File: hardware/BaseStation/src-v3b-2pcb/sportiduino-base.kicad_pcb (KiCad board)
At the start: 2 copper layers, 73 x 45 mm, 46 parts, among them SW1 SW_Reed, X1 Battery, X2 Prog, X3 RC522, X4 MINI RC522, X5 Charge

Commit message: Files for JLCPCB assemble
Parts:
- added  : hole, Sportiduino:hole, F.Cu at (196.0, 107.4)
- added  : hole, Sportiduino:hole, F.Cu at (190.0, 103.4)
- added  : hole, Sportiduino:hole, F.Cu at (191.5, 103.4)
- added  : hole, Sportiduino:hole, F.Cu at (193.0, 103.4)
- added  : hole, Sportiduino:hole, F.Cu at (194.5, 103.4)
- added  : hole, Sportiduino:hole, F.Cu at (196.0, 103.4)
- added  : hole, Sportiduino:hole, F.Cu at (172.0, 107.4)
- added  : hole, Sportiduino:hole, F.Cu at (170.5, 107.4)
- added  : hole, Sportiduino:hole, F.Cu at (169.0, 107.4)
- added  : hole, Sportiduino:hole, F.Cu at (167.5, 107.4)
- added  : hole, Sportiduino:hole, F.Cu at (166.0, 107.4)
- added  : hole, Sportiduino:hole, F.Cu at (194.5, 107.4)
- added  : hole, Sportiduino:hole, F.Cu at (164.5, 107.4)
- added  : hole, Sportiduino:hole, F.Cu at (163.0, 107.4)
- added  : hole, Sportiduino:hole, F.Cu at (163.0, 103.4)
- added  : hole, Sportiduino:hole, F.Cu at (164.5, 103.4)
- added  : hole, Sportiduino:hole, F.Cu at (166.0, 103.4)
- added  : hole, Sportiduino:hole, F.Cu at (167.5, 103.4)
- added  : hole, Sportiduino:hole, F.Cu at (169.0, 103.4)
- added  : hole, Sportiduino:hole, F.Cu at (170.5, 103.4)
- added  : hole, Sportiduino:hole, F.Cu at (172.0, 103.4)
- added  : hole, Sportiduino:hole, F.Cu at (193.0, 107.4)
- added  : hole, Sportiduino:hole, F.Cu at (191.5, 107.4)
- added  : hole, Sportiduino:hole, F.Cu at (190.0, 107.4)
- added  : hole, Sportiduino:hole, F.Cu at (188.5, 107.4)
- added  : hole, Sportiduino:hole, F.Cu at (187.0, 107.4)
- added  : hole, Sportiduino:hole, F.Cu at (187.0, 103.4)
- added  : hole, Sportiduino:hole, F.Cu at (188.5, 103.4)
- added BZ1: TR1205Y, Buzzer_Beeper:MagneticBuzzer_ProSignal_ABT-410-RC, F.Cu at (200.0, 122.4)
- added C1: 100 nF, Capacitor_SMD:C_0805_2012Metric_Pad1.15x1.40mm_HandSolder, F.Cu at (160.5, 113.5)
- added C10: 100 nF, Capacitor_SMD:C_0805_2012Metric_Pad1.15x1.40mm_HandSolder, F.Cu at (164.0, 146.7)
- added C11: 10 uF, Capacitor_SMD:C_0805_2012Metric_Pad1.18x1.45mm_HandSolder, F.Cu at (197.3, 146.2)
- added C12: 10 uF, Capacitor_SMD:C_0805_2012Metric_Pad1.18x1.45mm_HandSolder, F.Cu at (186.0, 146.0)
- added C2: 4.7 uF, Capacitor_SMD:C_0805_2012Metric_Pad1.15x1.40mm_HandSolder, F.Cu at (181.0, 146.0)
- added C3: 4.7 uF, Capacitor_SMD:C_0805_2012Metric_Pad1.15x1.40mm_HandSolder, F.Cu at (175.0, 146.0)
- added C4: 100 nF, Capacitor_SMD:C_0805_2012Metric_Pad1.15x1.40mm_HandSolder, F.Cu at (161.8, 122.7)
- added C5: 100 nF, Capacitor_SMD:C_0805_2012Metric_Pad1.15x1.40mm_HandSolder, F.Cu at (148.8, 130.9)
- added C6: 100 nF, Capacitor_SMD:C_0805_2012Metric_Pad1.15x1.40mm_HandSolder, F.Cu at (148.8, 133.2)
- added C7: 100 nF, Capacitor_SMD:C_0805_2012Metric_Pad1.15x1.40mm_HandSolder, F.Cu at (153.8, 135.7)
- added C9: 100 nF, Capacitor_SMD:C_0805_2012Metric_Pad1.15x1.40mm_HandSolder, F.Cu at (161.5, 145.4)
- added D1: MCP1700-3302E, Package_TO_SOT_SMD:SOT-23_Handsoldering, F.Cu at (178.0, 145.7)
- added D2: ATmega328P-AU, Package_QFP:TQFP-32_7x7mm_P0.8mm, F.Cu at (156.0, 127.4)
- added D3: DS3231SN, Sportiduino:SOIC-16W_7.5x10.3mm_P1.27mm, F.Cu at (154.0, 145.5)
- added D4: 24LC256T-I/SN, Package_SO:SOIC-8_3.9x4.9mm_P1.27mm, F.Cu at (169.3, 146.2)
- added D5: TP4056, Sportiduino:TP4056_SOP-8-PP, F.Cu at (192.0, 146.7)
- added G***: LOGO, Sportiduino:logo, F.Cu at (175.8, 126.4)
- added R1: 10K, Resistor_SMD:R_0805_2012Metric_Pad1.15x1.40mm_HandSolder, F.Cu at (166.8, 140.0)
- added R10: 68K, Resistor_SMD:R_0805_2012Metric_Pad1.15x1.40mm_HandSolder, F.Cu at (145.0, 147.8)
- added R11: 3K3, Resistor_SMD:R_0805_2012Metric_Pad1.15x1.40mm_HandSolder, F.Cu at (145.5, 143.4)
- added R12: 1K, Resistor_SMD:R_0805_2012Metric_Pad1.20x1.40mm_HandSolder, B.Cu at (140.3, 135.9)
- added R13: 1K, Resistor_SMD:R_0805_2012Metric_Pad1.20x1.40mm_HandSolder, B.Cu at (140.3, 138.2)
- added R14: 3K3, Resistor_SMD:R_0805_2012Metric_Pad1.20x1.40mm_HandSolder, F.Cu at (197.3, 150.2)
- added R2: 100, Resistor_SMD:R_0805_2012Metric_Pad1.15x1.40mm_HandSolder, F.Cu at (141.8, 140.9)
- added R3: 10K, Resistor_SMD:R_0805_2012Metric_Pad1.15x1.40mm_HandSolder, F.Cu at (166.8, 142.1)
- added R4: 3K3, Resistor_SMD:R_0805_2012Metric_Pad1.15x1.40mm_HandSolder, F.Cu at (189.0, 110.5)
- added R5: 33K, Resistor_SMD:R_0805_2012Metric_Pad1.15x1.40mm_HandSolder, F.Cu at (191.4, 110.5)
- added R6: 33K, Resistor_SMD:R_0805_2012Metric_Pad1.15x1.40mm_HandSolder, F.Cu at (163.5, 119.2)
- added R8: 3K3, Resistor_SMD:R_0805_2012Metric_Pad1.15x1.40mm_HandSolder, F.Cu at (145.5, 141.4)
- added R9: 270K, Resistor_SMD:R_0805_2012Metric_Pad1.15x1.40mm_HandSolder, F.Cu at (145.0, 149.9)
- added REF**: hole, hole, F.Cu at (0.00, 0.00)
- added SW1: SW_Reed, Button_Switch_THT:SW_reed, B.Cu at (170.0, 109.5)
- added TP1: , TestPoint:TestPoint_THTPad_D1.5mm_Drill0.7mm, F.Cu at (147.5, 135.7)
- added TP2: , TestPoint:TestPoint_THTPad_D1.5mm_Drill0.7mm, F.Cu at (147.5, 138.7)
- added TP4: , TestPoint:TestPoint_THTPad_D1.5mm_Drill0.7mm, F.Cu at (160.3, 119.9)
- added TP5: , TestPoint:TestPoint_THTPad_D1.5mm_Drill0.7mm, F.Cu at (157.8, 119.9)
- added VD1: 3mm, LED_THT:LED_D3.0mm, B.Cu at (138.0, 143.3)
- added VD2: , LED_SMD:LED_0805_2012Metric_Pad1.15x1.40mm_HandSolder, B.Cu at (136.0, 135.9)
- added VD3: , LED_SMD:LED_0805_2012Metric_Pad1.15x1.40mm_HandSolder, B.Cu at (136.0, 138.2)
- added VT1: BSS138, Package_TO_SOT_SMD:SOT-23_Handsoldering, F.Cu at (195.9, 110.5)
- added X1: Battery, Connector_JST:JST_XH_B2B-XH-A_1x02_P2.50mm_Vertical, F.Cu at (203.5, 140.4)
- added X2: Prog, Connector_IDC:IDC-Header_2x05_P2.54mm_Vertical, F.Cu at (139.6, 131.9)
- added X3: RC522, Connector_PinHeader_2.54mm:PinHeader_1x08_P2.54mm_Vertical, B.Cu at (144.8, 138.9)
- added X4: MINI RC522, Connector_PinHeader_2.54mm:PinHeader_1x08_P2.54mm_Vertical, B.Cu at (167.0, 137.4)
- added X5: Charge, Connector_JST:JST_XH_B2B-XH-A_1x02_P2.50mm_Vertical, F.Cu at (203.5, 129.9)
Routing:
- net (no net): track 0.00 -> 1303.1 mm, vias 0 -> 76
- added copper zone on B.Cu, net (none)
- added copper zone on F.Cu, net (none)
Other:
- board size 73 x 45 mm -> 73 x 94 mm

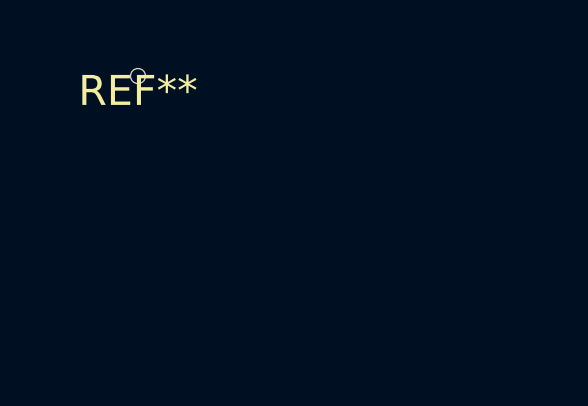
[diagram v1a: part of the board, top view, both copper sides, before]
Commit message: Updated BOM and pos files for BS PCB assembly
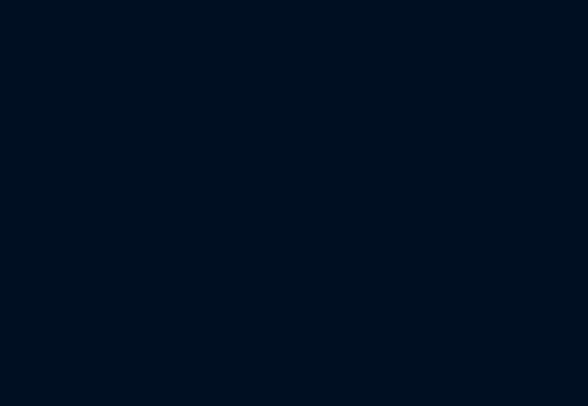
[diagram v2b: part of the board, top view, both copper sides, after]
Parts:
- removed REF**: hole, hole
- BZ1 (x2): value TR1205Y -> Passive Buzzer 12085 (12x8.5mm) 16 Ohm
- R14 (x2): value 3K3 -> 3K
- SW1 (x2): value SW_Reed -> Reed Switch Normally Open 2x14mm
- TP1 (x2), TP2 (x2), TP4 (x2), TP5 (x2): value (none) -> TestPoint (empty)
- VD1: value 3mm -> 1210 3528 BLUE 3.5x2.8x1.9mm
- VD1: value 3mm -> 1210 3528 BLUE 3.5*2.8*1.9mm
- VD2 (x2): value (none) -> 0805 GREEN
- VD3 (x2): value (none) -> 0805 RED
- X3 (x2): value RC522 -> Empty (RC522)
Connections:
- BZ1 pad 1: (no net) -> +BATT
- BZ1 pad 2: (no net) -> Net-(BZ1-Pad2)
- C1 pad 1: (no net) -> RST
- C1 pad 2: (no net) -> Net-(C1-Pad2)
- C10 pad 1: (no net) -> PD6
- C10 pad 2: (no net) -> GNDD
- C11 pad 1: (no net) -> Net-(C11-Pad1)
- C11 pad 2: (no net) -> GNDD
- C12 pad 1: (no net) -> +BATT
- C12 pad 2: (no net) -> GNDD
- C2 pad 1: (no net) -> +BATT
- C2 pad 2: (no net) -> GNDD
- C3 pad 1: (no net) -> +3V3
- C3 pad 2: (no net) -> GNDD
- C4 pad 1: (no net) -> +3V3
- C4 pad 2: (no net) -> GNDD
- C5 pad 1: (no net) -> +3V3
- C5 pad 2: (no net) -> GNDD
- C6 pad 1: (no net) -> Net-(C6-Pad1)
- C6 pad 2: (no net) -> GNDD
- C7 pad 1: (no net) -> ADCIN
- C7 pad 2: (no net) -> ADCEN
- C9 pad 1: (no net) -> +3V3
- C9 pad 2: (no net) -> GNDD
- D1 pad 1: (no net) -> GNDD
- D1 pad 2: (no net) -> +3V3
- D1 pad 3: (no net) -> +BATT
- D2 pad 1: (no net) -> /BUZ
- D2 pad 10: (no net) -> PD6
- D2 pad 11: (no net) -> Net-(D2-Pad11)
- D2 pad 12: (no net) -> /PB0
- D2 pad 13: (no net) -> /PB1
- D2 pad 14: (no net) -> /PB2
- D2 pad 15: (no net) -> PB3
- D2 pad 16: (no net) -> PB4
- D2 pad 17: (no net) -> PB5
- D2 pad 18: (no net) -> +3V3
- D2 pad 19: (no net) -> Net-(D2-Pad19)
- D2 pad 2: (no net) -> /LED
- D2 pad 20: (no net) -> Net-(C6-Pad1)
- D2 pad 21: (no net) -> GNDD
- D2 pad 22: (no net) -> Net-(D2-Pad22)
- D2 pad 23: (no net) -> ADCIN
- D2 pad 24: (no net) -> ADCEN
- D2 pad 25: (no net) -> ALARM
- D2 pad 26: (no net) -> PC3
- D2 pad 27: (no net) -> /SDA
- D2 pad 28: (no net) -> /SCL
- D2 pad 29: (no net) -> RST
- D2 pad 3: (no net) -> GNDD
- D2 pad 30: (no net) -> RX
- D2 pad 31: (no net) -> TX
- D2 pad 32: (no net) -> Net-(D2-Pad32)
- D2 pad 4: (no net) -> +3V3
- D2 pad 5: (no net) -> GNDD
- D2 pad 6: (no net) -> +3V3
- D2 pad 7: (no net) -> Net-(D2-Pad7)
- D2 pad 8: (no net) -> Net-(D2-Pad8)
- D2 pad 9: (no net) -> 32K
- D3 pad 1: (no net) -> 32K
- D3 pad 10: (no net) -> GNDD
- D3 pad 11: (no net) -> GNDD
- D3 pad 12: (no net) -> GNDD
- D3 pad 13: (no net) -> GNDD
- D3 pad 14: (no net) -> +3V3
- D3 pad 15: (no net) -> /SDA
- D3 pad 16: (no net) -> /SCL
- D3 pad 2: (no net) -> GNDD
- D3 pad 3: (no net) -> ALARM
- D3 pad 4: (no net) -> Net-(D2-Pad32)
- D3 pad 5: (no net) -> GNDD
- D3 pad 6: (no net) -> GNDD
- D3 pad 7: (no net) -> GNDD
- D3 pad 8: (no net) -> GNDD
- D3 pad 9: (no net) -> GNDD
- D4 pad 1: (no net) -> GNDD
- D4 pad 2: (no net) -> GNDD
- D4 pad 3: (no net) -> GNDD
- D4 pad 4: (no net) -> GNDD
- D4 pad 5: (no net) -> /SDA
- D4 pad 6: (no net) -> /SCL
- D4 pad 7: (no net) -> GNDD
- D4 pad 8: (no net) -> PD6
- D5 pad 1: (no net) -> GNDD
- D5 pad 2: (no net) -> Net-(D5-Pad2)
- D5 pad 3: (no net) -> GNDD
- D5 pad 4: (no net) -> Net-(C11-Pad1)
- D5 pad 5: (no net) -> +BATT
- D5 pad 6: (no net) -> Net-(D5-Pad6)
- D5 pad 7: (no net) -> Net-(D5-Pad7)
- D5 pad 8: (no net) -> Net-(C11-Pad1)
- D5 pad 9: (no net) -> GNDD
- R1 pad 1: (no net) -> +3V3
- R1 pad 2: (no net) -> /SCL
- R10 pad 1: (no net) -> ADCEN
- R10 pad 2: (no net) -> ADCIN
- R11 pad 1: (no net) -> +3V3
- R11 pad 2: (no net) -> ALARM
- R12 pad 1: (no net) -> Net-(D5-Pad6)
- R12 pad 2: (no net) -> Net-(R12-Pad2)
- R13 pad 1: (no net) -> Net-(D5-Pad7)
- R13 pad 2: (no net) -> Net-(R13-Pad2)
- R14 pad 1: (no net) -> GNDD
- R14 pad 2: (no net) -> Net-(D5-Pad2)
- R2 pad 1: (no net) -> Net-(R2-Pad1)
- R2 pad 2: (no net) -> /LED
- R3 pad 1: (no net) -> +3V3
- R3 pad 2: (no net) -> /SDA
- R4 pad 1: (no net) -> Net-(R4-Pad1)
- R4 pad 2: (no net) -> /BUZ
- R5 pad 1: (no net) -> GNDD
- R5 pad 2: (no net) -> Net-(R4-Pad1)
- R6 pad 1: (no net) -> +3V3
- R6 pad 2: (no net) -> RST
- R8 pad 1: (no net) -> +3V3
- R8 pad 2: (no net) -> 32K
- R9 pad 1: (no net) -> ADCIN
- R9 pad 2: (no net) -> +BATT
- SW1 pad 1: (no net) -> Net-(D2-Pad11)
- SW1 pad 2: (no net) -> GNDD
- TP1 pad 1: (no net) -> Net-(D2-Pad19)
- TP2 pad 1: (no net) -> Net-(D2-Pad22)
- TP4 pad 1: (no net) -> Net-(D2-Pad7)
- TP5 pad 1: (no net) -> Net-(D2-Pad8)
- VD1 pad 1: (no net) -> GNDD
- VD1 pad 2: (no net) -> Net-(R2-Pad1)
- VD2 pad 1: (no net) -> Net-(R12-Pad2)
- VD2 pad 2: (no net) -> Net-(C11-Pad1)
- VD3 pad 1: (no net) -> Net-(R13-Pad2)
- VD3 pad 2: (no net) -> Net-(C11-Pad1)
- VT1 pad 1: (no net) -> Net-(R4-Pad1)
- VT1 pad 2: (no net) -> GNDD
- VT1 pad 3: (no net) -> Net-(BZ1-Pad2)
- X1 pad 1: (no net) -> GNDD
- X1 pad 2: (no net) -> +BATT
- X2 pad 1: (no net) -> GNDD
- X2 pad 10: (no net) -> PB3
- X2 pad 2: (no net) -> +3V3
- X2 pad 3: (no net) -> PC3
- X2 pad 4: (no net) -> Net-(C1-Pad2)
- X2 pad 5: (no net) -> TX
- X2 pad 6: (no net) -> RX
- X2 pad 7: (no net) -> RST
- X2 pad 8: (no net) -> PB5
- X2 pad 9: (no net) -> PB4
- X3 pad 1: (no net) -> +3V3
- X3 pad 2: (no net) -> /PB1
- X3 pad 3: (no net) -> GNDD
- X3 pad 4: (no net) -> /PB0
- X3 pad 5: (no net) -> PB4
- X3 pad 6: (no net) -> PB3
- X3 pad 7: (no net) -> PB5
- X3 pad 8: (no net) -> /PB2
- X4 pad 1: (no net) -> +3V3
- X4 pad 2: (no net) -> /PB1
- X4 pad 3: (no net) -> GNDD
- X4 pad 4: (no net) -> /PB0
- X4 pad 5: (no net) -> PB4
- X4 pad 6: (no net) -> PB3
- X4 pad 7: (no net) -> PB5
- X4 pad 8: (no net) -> /PB2
- X5 pad 1: (no net) -> GNDD
- X5 pad 2: (no net) -> Net-(C11-Pad1)
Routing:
- net (no net): track 1303.1 -> 0.00 mm, vias 76 -> 0
- net +3V3: track 114.9 -> 229.8 mm, vias 5 -> 10
- net Net-(C11-Pad1): track 98.0 -> 196.0 mm, vias 2 -> 4
- net GNDD: track 72.1 -> 144.3 mm, vias 32 -> 64
- net Net-(D5-Pad6): track 58.8 -> 117.6 mm, vias 1 -> 2
- net Net-(D5-Pad7): track 56.7 -> 113.4 mm, vias 1 -> 2
- net PB5: track 56.4 -> 112.9 mm, vias 2 -> 4
- net +BATT: track 54.0 -> 107.9 mm
- net PD6: track 52.8 -> 105.5 mm, vias 2 -> 4
- net RST: track 52.7 -> 105.4 mm, vias 2 -> 4
- net /PB1: track 49.1 -> 98.2 mm, vias 1 -> 2
- net /PB0: track 45.3 -> 90.5 mm, vias 2 -> 4
- net PB3: track 43.1 -> 86.3 mm, vias 1 -> 2
- net /PB2: track 42.2 -> 84.4 mm
- net Net-(C1-Pad2): track 41.1 -> 82.2 mm, vias 1 -> 2
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- removed copper zone on B.Cu, net (none)
- removed copper zone on F.Cu, net (none)

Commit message: Fix docs
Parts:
- BZ1 (x2): value Passive Buzzer 12085 (12x8.5mm) 16 Ohm -> Passive Buzzer 12085 (12x8.5mm) 16 ohm
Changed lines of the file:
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@@
       (effects (font (size 1 1) (thickness 0.15)))
     )
-    (fp_text value "Passive Buzzer 12085 (12x8.5mm) 16 Ohm" (at 3.302 3.81 90) (layer F.Fab)
+    (fp_text value "Passive Buzzer 12085 (12x8.5mm) 16 ohm" (at 3.302 3.81 90) (layer F.Fab)
       (effects (font (size 1 1) (thickness 0.15)))
     )
@@
       (effects (font (size 1 1) (thickness 0.15)))
     )
-    (fp_text value "Passive Buzzer 12085 (12x8.5mm) 16 Ohm" (at 3.302 3.81 90) (layer F.Fab)
-      (effects (font (size 1 1) (thickness 0.15)))
-    )
+    (fp_text value "Passive Buzzer 12085 (12x8.5mm) 16 ohm" (at 3.302 3.81 90) (layer F.Fab)
+      (effects (font (size 1 1) (thickness 0.15)))
+    )
